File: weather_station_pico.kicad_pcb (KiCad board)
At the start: 2 copper layers, 90.2 x 90.2 mm, 28 parts, among them J1 POWER, J2 WSPEED, J3 WDIR, J4 I2C, SW1 SW_Push, U1 LM7805_TO220, U2 E220-900T22D, U3 Pico, U4 74HC4051, U5 LM35-LP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

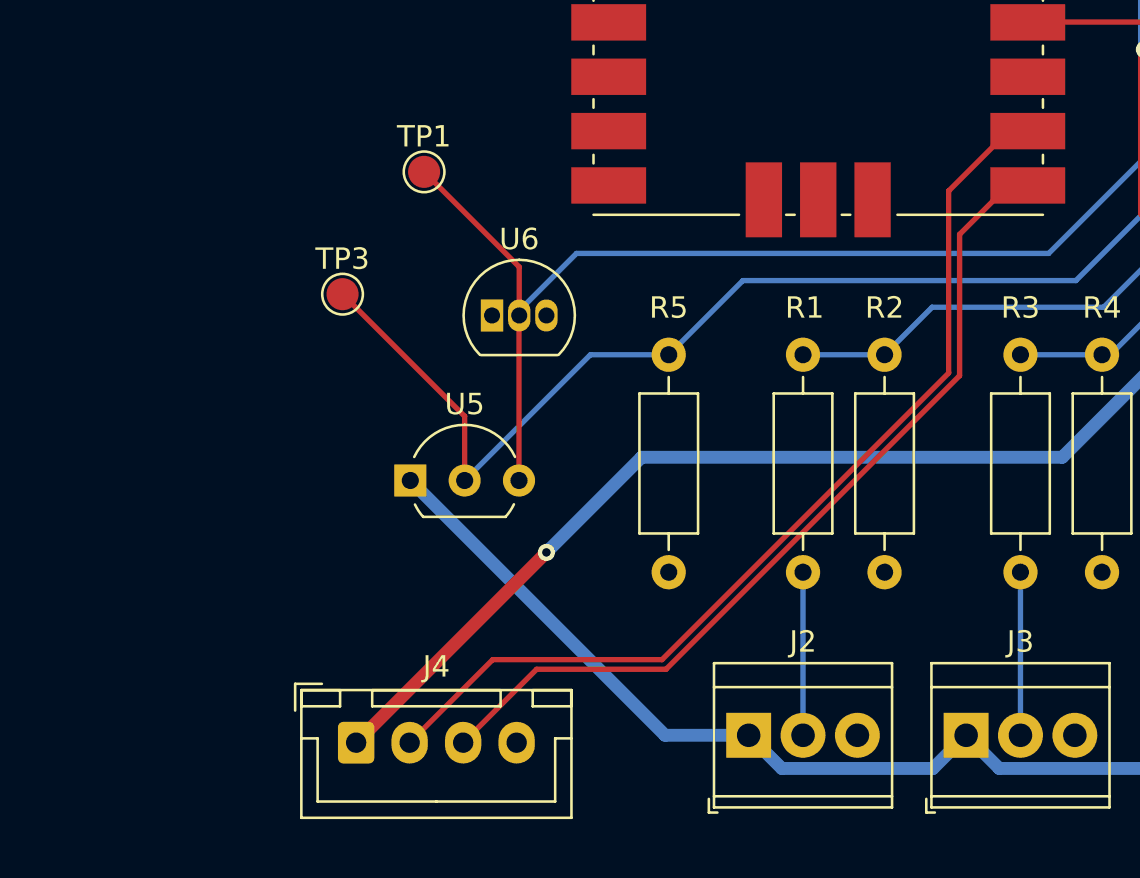
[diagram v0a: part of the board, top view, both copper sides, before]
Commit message: add i2c pull-up resistors
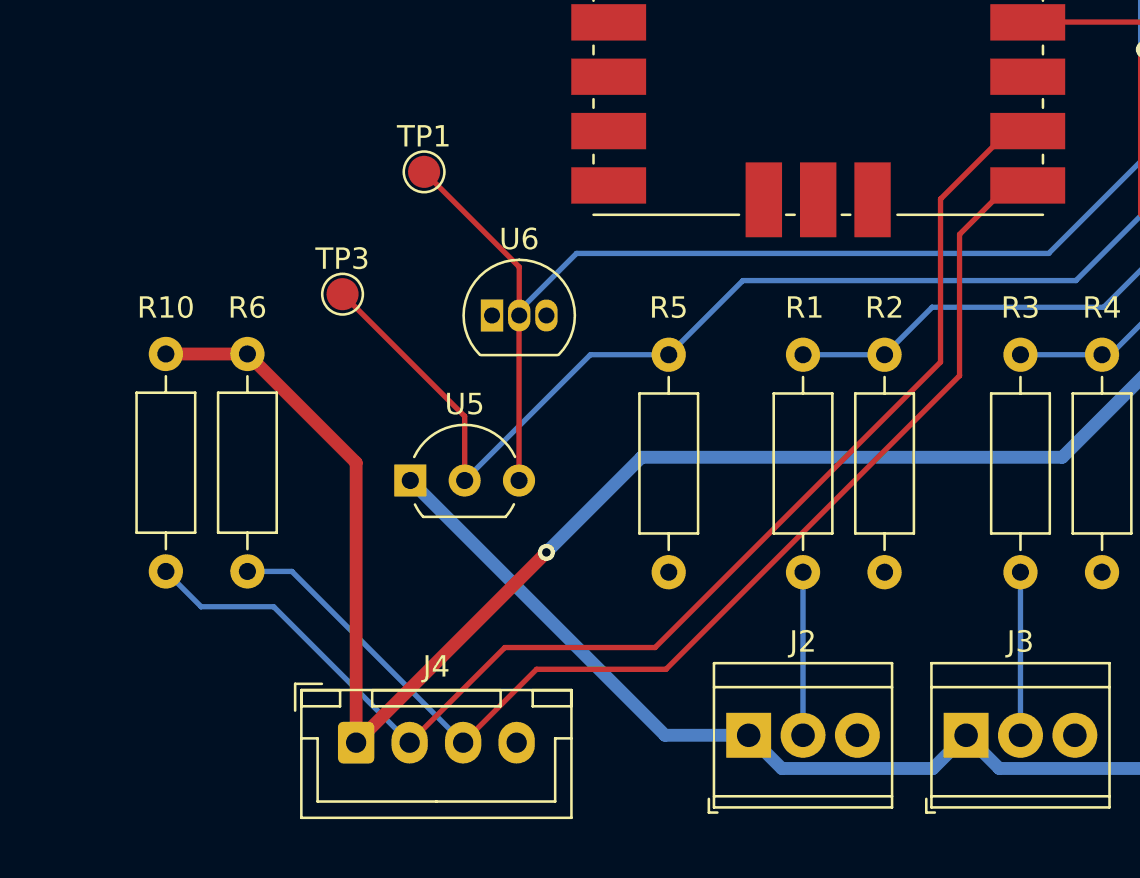
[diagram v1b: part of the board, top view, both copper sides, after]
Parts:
- added R10: 10K, Resistor_THT:R_Axial_DIN0207_L6.3mm_D2.5mm_P10.16mm_Horizontal, F.Cu at (88.9, 118.4)
- added R6: 10K, Resistor_THT:R_Axial_DIN0207_L6.3mm_D2.5mm_P10.16mm_Horizontal, F.Cu at (92.7, 118.4)
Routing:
- net +3V3: track 98.5 -> 122.6 mm
- net /SCL: track 44.8 -> 59.0 mm
- net /SDA: track 40.1 -> 53.5 mm
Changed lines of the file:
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@@
+    )
+  )
+  (footprint "Resistor_THT:R_Axial_DIN0207_L6.3mm_D2.5mm_P10.16mm_Horizontal" (layer "F.Cu")
+    (at 88.9 118.364 -90)
+    (descr "Resistor, Axial_DIN0207 series, Axial, Horizontal, pin pitch=10.16mm, 0.25W = 1/4W, length*diameter=6.3*2.5mm^2, http://cdn-reichelt.de/documents/datenblatt/B400/1_4W%23YAG.pdf")
+    (tags "Resistor Axial_DIN0207 series Axial Horizontal pin pitch 10.16mm 0.25W = 1/4W length 6.3mm diameter 2.5mm")
+    (property "Sheetfile" "weather_station_pico.kicad_sch")
+    (property "Sheetname" "")
+    (attr through_hole)
+    (fp_text reference "R10" (at -2.159 0 180) (layer "F.SilkS")
+      (effects (font (size 1 1) (thickness 0.15)))
+    )
+    (fp_text value "10K" (at 5.08 0 90) (layer "F.Fab")
+      (effects (font (size 1 1) (thickness 0.15)))
+    )
+    (fp_text user "${REFERENCE}" (at 1.016 2.54 180) (layer "F.Fab")
+      (effects (font (size 1 1) (thickness 0.15)))
+    )
+    (fp_line (start 1.81 1.37) (end 8.35 1.37) (layer "F.SilkS") (width 0.12))
+    (fp_line (start 9.12 0) (end 8.35 0) (layer "F.SilkS") (width 0.12))
+    (fp_line (start 8.35 -1.37) (end 1.81 -1.37) (layer "F.SilkS") (width 0.12))
+    (fp_line (start 1.81 -1.37) (end 1.81 1.37) (layer "F.SilkS") (width 0.12))
+    (fp_line (start 8.35 1.37) (end 8.35 -1.37) (layer "F.SilkS") (width 0.12))
+    (fp_line (start 1.04 0) (end 1.81 0) (layer "F.SilkS") (width 0.12))
+    (fp_line (start -1.05 1.5) (end 11.21 1.5) (layer "F.CrtYd") (width 0.05))
+    (fp_line (start -1.05 -1.5) (end -1.05 1.5) (layer "F.CrtYd") (width 0.05))
+    (fp_line (start 11.21 -1.5) (end -1.05 -1.5) (layer "F.CrtYd") (width 0.05))
+    (fp_line (start 11.21 1.5) (end 11.21 -1.5) (layer "F.CrtYd") (width 0.05))
+    (fp_line (start 0 0) (end 1.93 0) (layer "F.Fab") (width 0.1))
+    (fp_line (start 10.16 0) (end 8.23 0) (layer "F.Fab") (width 0.1))
+    (fp_line (start 8.23 1.25) (end 8.23 -1.25) (layer "F.Fab") (width 0.1))
+    (fp_line (start 1.93 1.25) (end 8.23 1.25) (layer "F.Fab") (width 0.1))
+    (fp_line (start 1.93 -1.25) (end 1.93 1.25) (layer "F.Fab") (width 0.1))
+    (fp_line (start 8.23 -1.25) (end 1.93 -1.25) (layer "F.Fab") (width 0.1))
+    (pad "1" thru_hole circle (at 0 0 270) (size 1.6 1.6) (drill 0.8) (layers *.Cu *.Mask)
+      (net 33 "+3V3") (pintype "passive"))
+    (pad "2" thru_hole oval (at 10.16 0 270) (size 1.6 1.6) (drill 0.8) (layers *.Cu *.Mask)
+      (net 45 "/SCL") (pintype "passive"))
+    (model "${KICAD6_3DMODEL_DIR}/Resistor_THT.3dshapes/R_Axial_DIN0207_L6.3mm_D2.5mm_P10.16mm_Horizontal.wrl"
+      (offset (xyz 0 0 0))
+      (scale (xyz 1 1 1))
+      (rotate (xyz 0 0 0))
     )
   )
@@
       (effects (font (size 1 1) (thickness 0.15)))
     )
-    (fp_text value "TEMP_OUT" (at 0 1.75) (layer "F.Fab")
+    (fp_text value "TEMP_OUT" (at 1.27 1.905) (layer "F.Fab")
       (effects (font (size 1 1) (thickness 0.15)))
     )
@@
     )
   )
+  (footprint "Resistor_THT:R_Axial_DIN0207_L6.3mm_D2.5mm_P10.16mm_Horizontal" (layer "F.Cu")
+    (at 92.71 118.364 -90)
+    (descr "Resistor, Axial_DIN0207 series, Axial, Horizontal, pin pitch=10.16mm, 0.25W = 1/4W, length*diameter=6.3*2.5mm^2, http://cdn-reichelt.de/documents/datenblatt/B400/1_4W%23YAG.pdf")
+    (tags "Resistor Axial_DIN0207 series Axial Horizontal pin pitch 10.16mm 0.25W = 1/4W length 6.3mm diameter 2.5mm")
+    (property "Sheetfile" "weather_station_pico.kicad_sch")
+    (property "Sheetname" "")
+    (attr through_hole)
+    (fp_text reference "R6" (at -2.159 0 180) (layer "F.SilkS")
+      (effects (font (size 1 1) (thickness 0.15)))
+    )
+    (fp_text value "10K" (at 5.08 0 90) (layer "F.Fab")
+      (effects (font (size 1 1) (thickness 0.15)))
+    )
+    (fp_text user "${REFERENCE}" (at 1.016 -1.905 180) (layer "F.Fab")
+      (effects (font (size 1 1) (thickness 0.15)))
+    )
+    (fp_line (start 1.04 0) (end 1.81 0) (layer "F.SilkS") (width 0.12))
+    (fp_line (start 1.81 -1.37) (end 1.81 1.37) (layer "F.SilkS") (width 0.12))
+    (fp_line (start 8.35 -1.37) (end 1.81 -1.37) (layer "F.SilkS") (width 0.12))
+    (fp_line (start 1.81 1.37) (end 8.35 1.37) (layer "F.SilkS") (width 0.12))
+    (fp_line (start 8.35 1.37) (end 8.35 -1.37) (layer "F.SilkS") (width 0.12))
+    (fp_line (start 9.12 0) (end 8.35 0) (layer "F.SilkS") (width 0.12))
+    (fp_line (start -1.05 -1.5) (end -1.05 1.5) (layer "F.CrtYd") (width 0.05))
+    (fp_line (start -1.05 1.5) (end 11.21 1.5) (layer "F.CrtYd") (width 0.05))
+    (fp_line (start 11.21 1.5) (end 11.21 -1.5) (layer "F.CrtYd") (width 0.05))
+    (fp_line (start 11.21 -1.5) (end -1.05 -1.5) (layer "F.CrtYd") (width 0.05))
+    (fp_line (start 1.93 1.25) (end 8.23 1.25) (layer "F.Fab") (width 0.1))
+    (fp_line (start 10.16 0) (end 8.23 0) (layer "F.Fab") (width 0.1))
+    (fp_line (start 1.93 -1.25) (end 1.93 1.25) (layer "F.Fab") (width 0.1))
+    (fp_line (start 8.23 -1.25) (end 1.93 -1.25) (layer "F.Fab") (width 0.1))
+    (fp_line (start 8.23 1.25) (end 8.23 -1.25) (layer "F.Fab") (width 0.1))
+    (fp_line (start 0 0) (end 1.93 0) (layer "F.Fab") (width 0.1))
+    (pad "1" thru_hole circle (at 0 0 270) (size 1.6 1.6) (drill 0.8) (layers *.Cu *.Mask)
+      (net 33 "+3V3") (pintype "passive"))
+    (pad "2" thru_hole oval (at 10.16 0 270) (size 1.6 1.6) (drill 0.8) (layers *.Cu *.Mask)
+      (net 44 "/SDA") (pintype "passive"))
+    (model "${KICAD6_3DMODEL_DIR}/Resistor_THT.3dshapes/R_Axial_DIN0207_L6.3mm_D2.5mm_P10.16mm_Horizontal.wrl"
+      (offset (xyz 0 0 0))
+      (scale (xyz 1 1 1))
+      (rotate (xyz 0 0 0))
+    )
+  )
   (footprint "Capacitor_THT:C_Disc_D5.0mm_W2.5mm_P5.00mm" (layer "F.Cu")
     (at 137.16 66.675 -90)
@@
   (segment (start 134.62 86.36) (end 134.62 75.565) (width 0.6) (layer "F.Cu") (net 33))
   (segment (start 134.62 75.565) (end 131.445 72.39) (width 0.6) (layer "F.Cu") (net 33))
+  (segment (start 97.79 136.525) (end 97.79 123.444) (width 0.6) (layer "F.Cu") (net 33))
   (segment (start 134.62 111.755) (end 138.42 115.555) (width 0.6) (layer "F.Cu") (net 33))
   (segment (start 97.79 136.525) (end 106.68 127.635) (width 0.6) (layer "F.Cu") (net 33))
+  (segment (start 97.79 123.444) (end 92.71 118.364) (width 0.6) (layer "F.Cu") (net 33))
+  (segment (start 88.9 118.364) (end 92.71 118.364) (width 0.6) (layer "F.Cu") (net 33))
   (via (at 134.62 86.36) (size 0.8) (drill 0.4) (layers "F.Cu" "B.Cu") (net 33))
   (via (at 134.62 104.14) (size 0.8) (drill 0.4) (layers "F.Cu" "B.Cu") (net 33))
@@
   (segment (start 128.27 110.49) (end 125.984 112.776) (width 0.25) (layer "F.Cu") (net 44))
   (segment (start 125.984 112.776) (end 125.984 119.38) (width 0.25) (layer "F.Cu") (net 44))
-  (segment (start 125.476 110.744) (end 125.476 119.252282) (width 0.25) (layer "F.Cu") (net 45))
-  (segment (start 125.476 119.252282) (end 112.081802 132.64648) (width 0.25) (layer "F.Cu") (net 45))
-  (segment (start 112.081802 132.64648) (end 104.16852 132.64648) (width 0.25) (layer "F.Cu") (net 45))
-  (segment (start 128.27 107.95) (end 125.476 110.744) (width 0.25) (layer "F.Cu") (net 45))
-  (segment (start 104.16852 132.64648) (end 100.29 136.525) (width 0.25) (layer "F.Cu") (net 45))
+  (segment (start 92.71 128.524) (end 94.789 128.524) (width 0.25) (layer "B.Cu") (net 44))
+  (segment (start 94.789 128.524) (end 102.79 136.525) (width 0.25) (layer "B.Cu") (net 44))
+  (segment (start 111.76 132.08) (end 125.095 118.745) (width 0.25) (layer "F.Cu") (net 45))
+  (segment (start 104.735 132.08) (end 111.76 132.08) (width 0.25) (layer "F.Cu") (net 45))
+  (segment (start 125.095 111.125) (end 128.27 107.95) (width 0.25) (layer "F.Cu") (net 45))
+  (segment (start 125.095 118.745) (end 125.095 111.125) (width 0.25) (layer "F.Cu") (net 45))
+  (segment (start 100.29 136.525) (end 104.735 132.08) (width 0.25) (layer "F.Cu") (net 45))
+  (segment (start 90.551 130.175) (end 93.94 130.175) (width 0.25) (layer "B.Cu") (net 45))
+  (segment (start 93.94 130.175) (end 100.29 136.525) (width 0.25) (layer "B.Cu") (net 45))
+  (segment (start 88.9 128.524) (end 90.551 130.175) (width 0.25) (layer "B.Cu") (net 45))
   (zone (net 2) (net_name "GND") (layer "F.Cu") (hatch edge 0.508)
     (connect_pads (clearance 0.508))

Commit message: ready for plot
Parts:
- moved H3 50.2 mm to (118.9, 65.7)
- moved H4 50.2 mm to (118.9, 148.7)
- moved H1 48.7 mm to (200.4, 148.7)
- moved H2 48.7 mm to (200.4, 65.7)
- moved J1 48.6 mm to (191.8, 141.9)
- moved R4 48.6 mm to (180.9, 124.1)
- moved U4 48.6 mm to (194.3, 121.3)
- moved U5 48.6 mm to (148.6, 130.0)
- moved J3 48.6 mm to (174.6, 141.9)
- moved J4 48.6 mm to (146.1, 142.2)
- moved R1 48.6 mm to (166.9, 134.3)
- moved R2 48.6 mm to (170.7, 124.1)
- moved R5 48.6 mm to (160.7, 124.1)
- moved R6 48.6 mm to (141.0, 124.1)
- moved R7 48.6 mm to (144.8, 106.0)
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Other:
- board size 90.2 x 90.2 mm -> 88.5 x 90 mm
- board text added: "WS v1.0 by M.E.M."

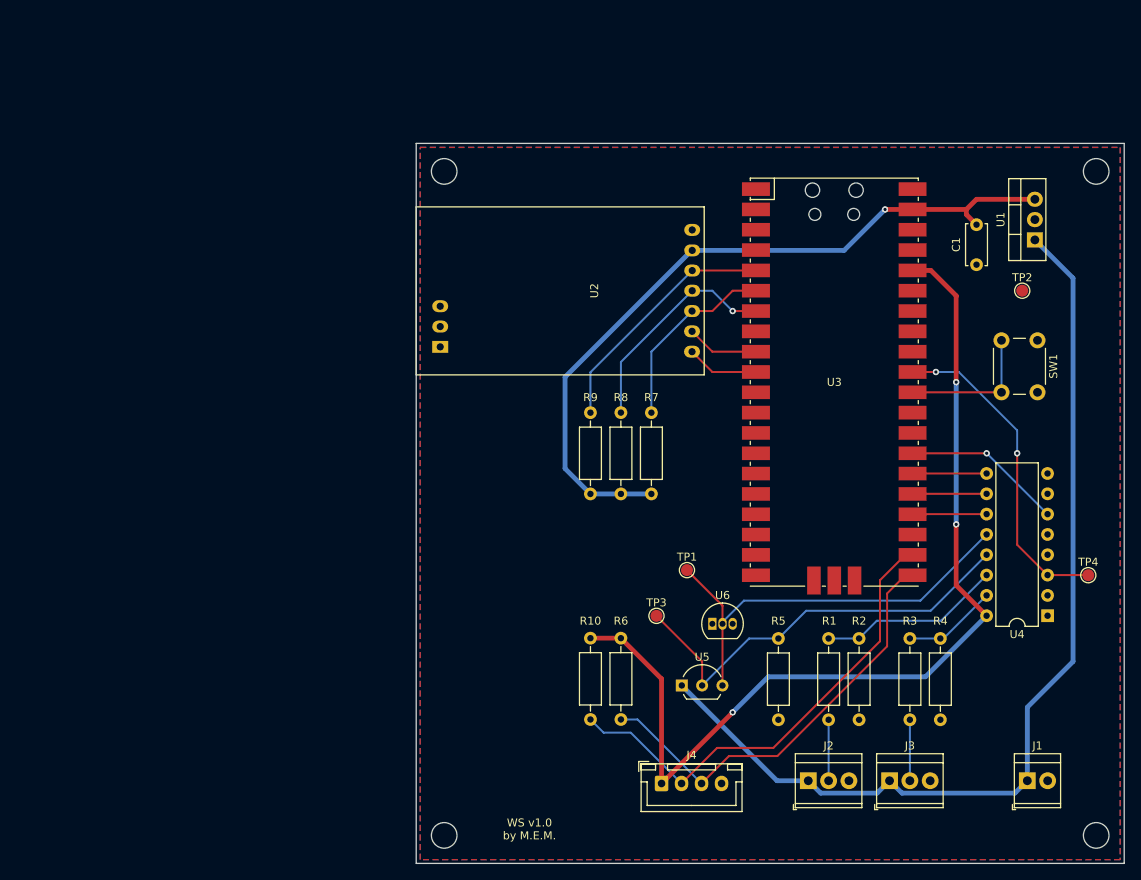
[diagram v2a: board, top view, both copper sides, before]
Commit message: remove a via
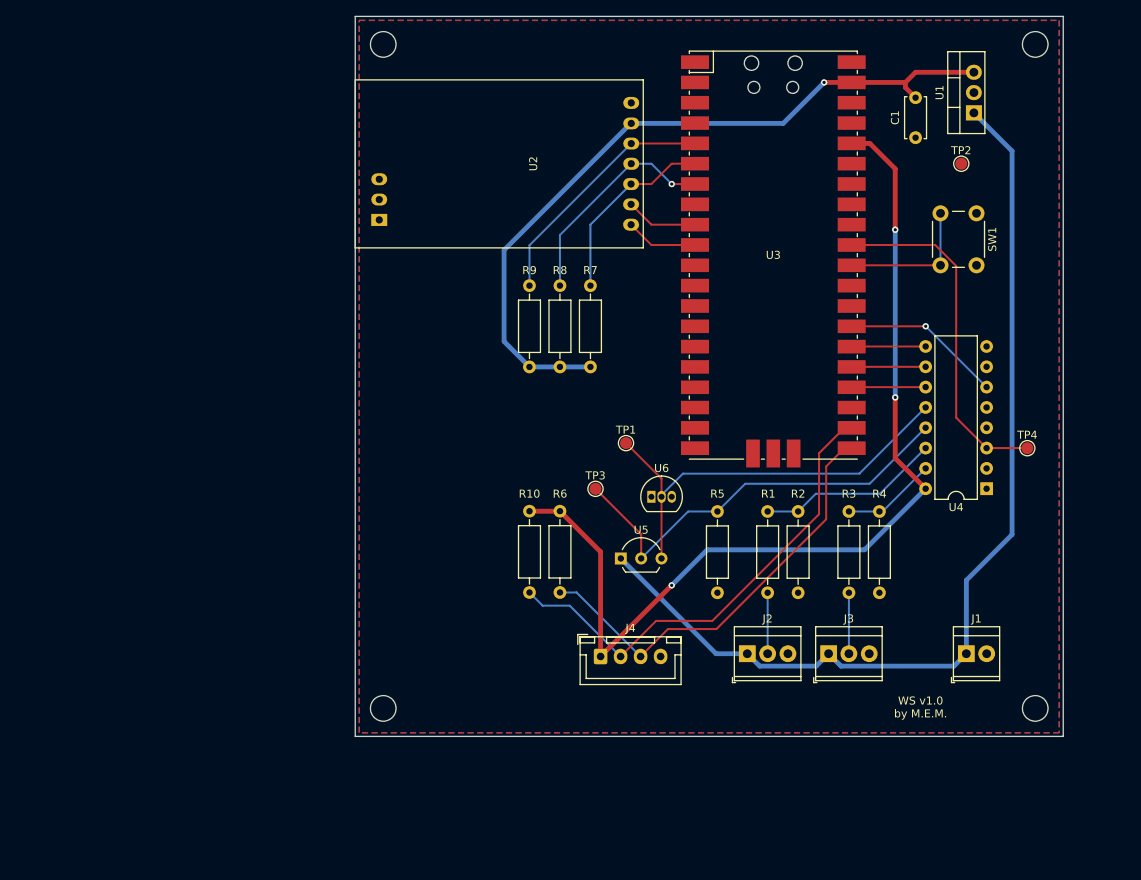
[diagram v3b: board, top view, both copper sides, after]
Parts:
- moved J1 17.6 mm to (184.2, 126.0)
- moved J3 17.6 mm to (166.9, 126.0)
- moved J4 17.6 mm to (138.4, 126.4)
- moved U5 17.6 mm to (141.0, 114.1)
- moved H2 17.6 mm to (192.8, 49.9)
- moved H3 17.6 mm to (111.3, 49.9)
- moved H1 17.6 mm to (192.8, 132.9)
- moved H4 17.6 mm to (111.3, 132.9)
- moved J2 17.6 mm to (156.8, 126.0)
- moved R1 17.6 mm to (159.3, 118.4)
- moved R10 17.6 mm to (129.5, 108.2)
- moved R2 17.6 mm to (163.1, 108.2)
- moved R3 17.6 mm to (169.5, 118.4)
- moved R4 17.6 mm to (173.3, 108.2)
- moved R5 17.6 mm to (153.0, 108.2)
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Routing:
- net /MUX_ADC: track 41.7 -> 44.5 mm, vias 2 -> 0
